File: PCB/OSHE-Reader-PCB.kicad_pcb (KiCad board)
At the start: 4 copper layers, 115 x 100 mm, 82 parts, among them J1 2171750001, J2 112L-TDA0, J3 Conn_01x24_MountingPin, J4 S2B-PH-K-SLFSN, Q1 PNP, Q2 Si1308EDL, SW1 SW_Push, SW2 SW_Push, SW3 SW_Push, SW4 SW_Push, SW5 SW_Push, U1 BQ2057CSNTR, U2 IRF7326D2TRPBF, U3 TPS5432DDA

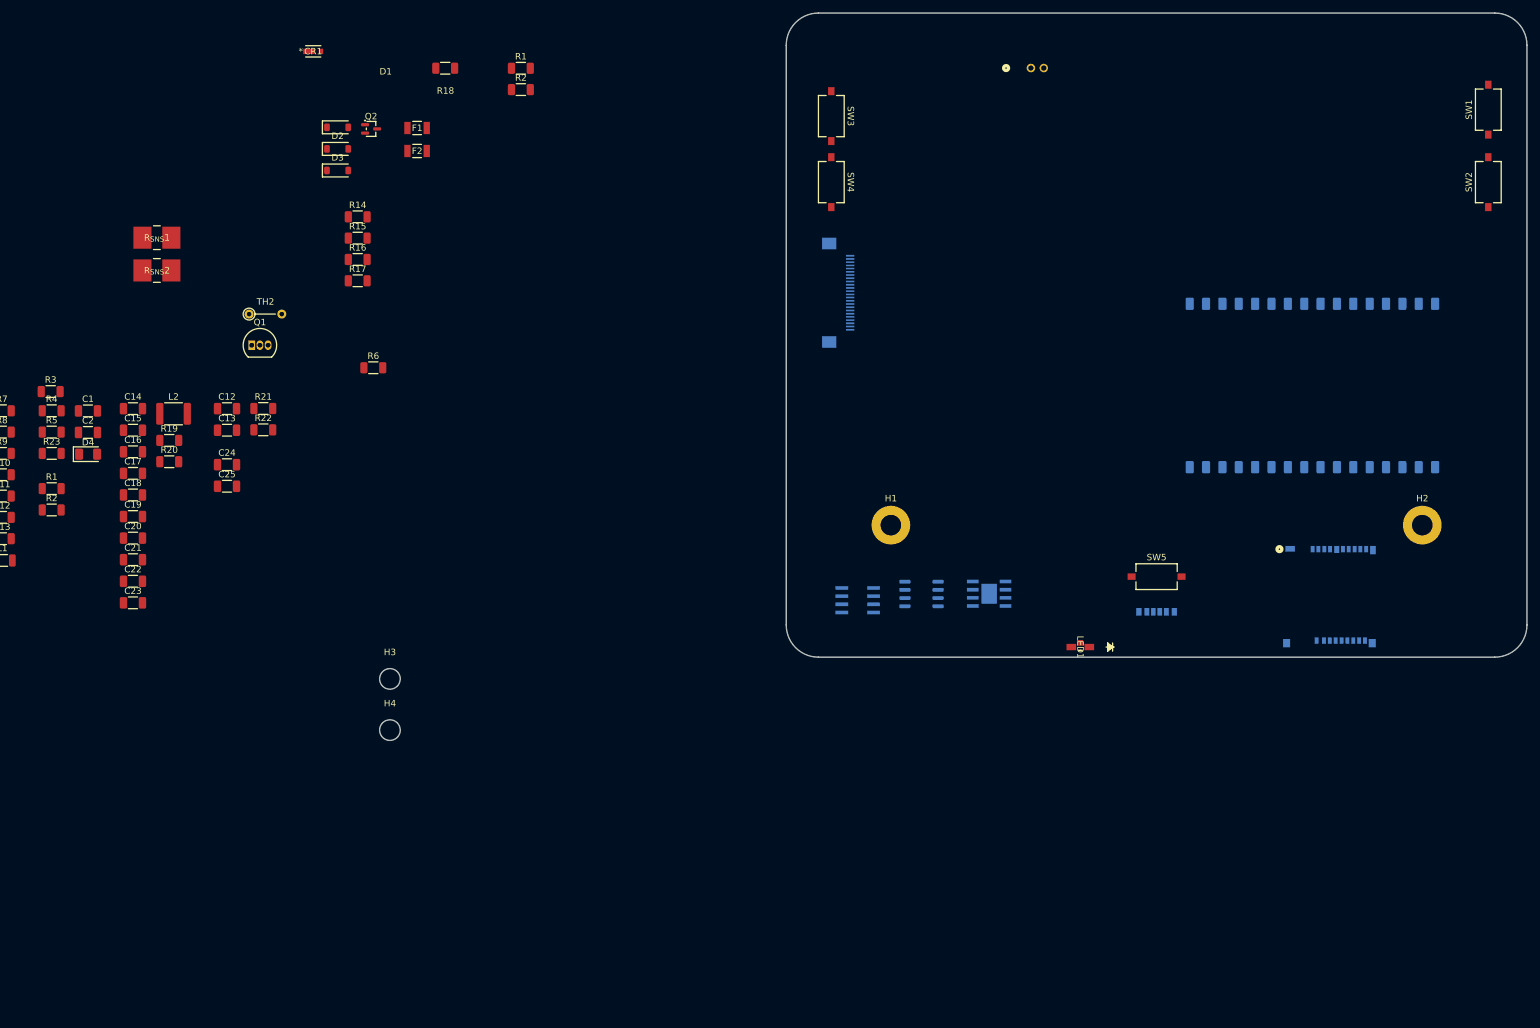
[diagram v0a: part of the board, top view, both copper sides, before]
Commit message: Started routing PCB & added case dxf for reference
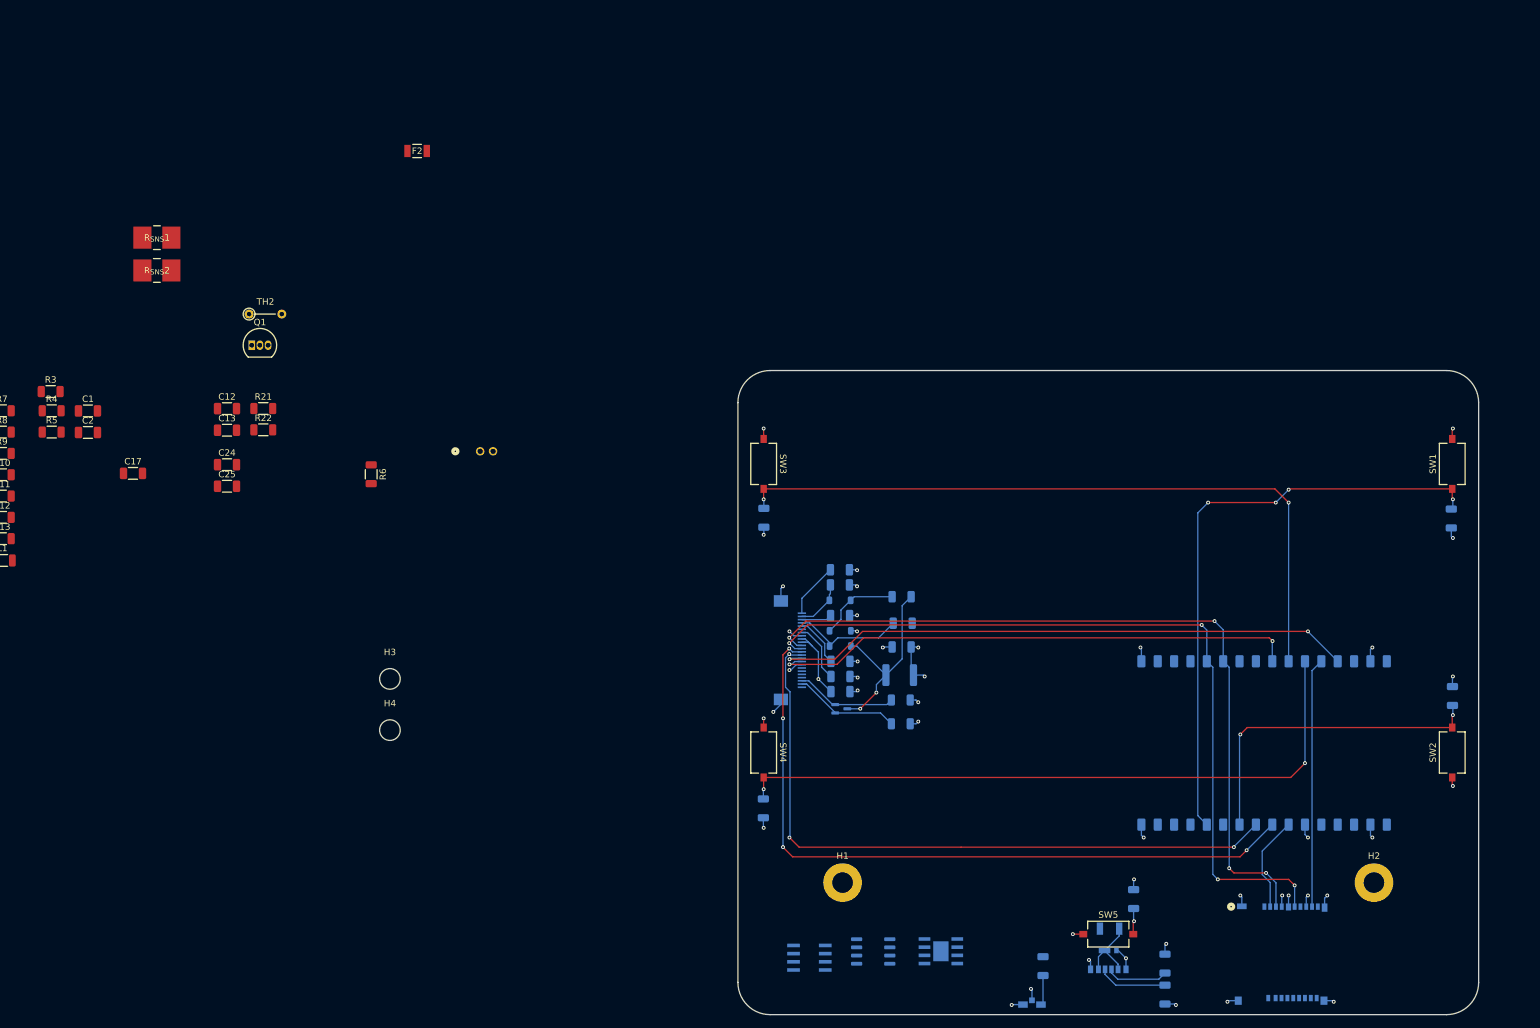
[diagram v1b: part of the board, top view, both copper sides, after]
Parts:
- removed D4: LED, LED_SMD:LED_1206_3216Metric
- removed the R1 at (-74.0, 98.8)
- removed the R2 at (-74.0, 102.1)
- C14, C15, C16, C18, C19, C20, C21, C22, C23, CR1, D1, D2, D3, F1, L2, LED1, Q2, R1, R14, R15, R16, R17, R18, R19, R2, R20, R23: moved to B.Cu
- moved CR1 186.4 mm to (90.1, 170.6)
- moved R17 181.8 mm to (143.4, 131.0), turned to 90 degrees
- moved R16 174.5 mm to (143.3, 103.5), turned to -90 degrees
- moved R23 173.3 mm to (79.9, 173.0), turned to -90 degrees
- moved R2 172.5 mm to (98.8, 177.4), turned to -90 degrees
- moved R1 171.2 mm to (98.8, 172.6), turned to -90 degrees
- moved R18 167.5 mm to (93.9, 162.6), turned to 90 degrees
- moved F1 164.3 mm to (90.2, 167.2), turned to 180 degrees
- moved C14 124.9 mm to (57.9, 123.4), turned to 180 degrees
- moved C15 123.2 mm to (58.1, 119.7)
- moved C16 121.4 mm to (57.9, 115.6)
- moved R20 120.6 mm to (57.8, 135.3)
- moved R19 120.5 mm to (57.8, 131.7)
- moved L2 119.8 mm to (57.6, 127.8), turned to 180 degrees
- moved Q2 115.9 mm to (48.5, 133.0)
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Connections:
- J3 pad 25: unconnected-(J3-Pad25) -> GND
- J3 pad 26: unconnected-(J3-Pad26) -> GND
- LED1 pad 2: unconnected-(LED1-Pad2) -> GND
- SW1 pad 1: +3V3 -> /Buttons/LeftButton
- SW1 pad 2: /Buttons/LeftButton -> +3V3
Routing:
- net /SCK: track 0.00 -> 123.7 mm, vias 0 -> 4
- net /COPI: track 0.00 -> 120.8 mm, vias 0 -> 4
- net /EP_CS: track 0.00 -> 112.1 mm, vias 0 -> 4
- net /Buttons/UpButton: track 0.00 -> 110.1 mm, vias 0 -> 2
- net /EP_D/C: track 0.00 -> 105.6 mm, vias 0 -> 3
- net /Buttons/DownButton: track 0.00 -> 104.1 mm, vias 0 -> 2
- net /Buttons/LeftButton: track 0.00 -> 93.3 mm, vias 0 -> 4
- net /EP_RESET: track 0.00 -> 91.0 mm, vias 0 -> 2
- net /EP_BUSY: track 0.00 -> 82.2 mm, vias 0 -> 2
- net GND: track 0.00 -> 61.5 mm, vias 0 -> 35
- net /Buttons/RightButton: track 0.00 -> 50.9 mm, vias 0 -> 2
- net /CIPO: track 0.00 -> 38.7 mm
- net +3V3: track 0.00 -> 31.3 mm, vias 0 -> 10
- net Net-(D2-A): track 0.00 -> 30.0 mm, vias 0 -> 2
- net /Display Connector/PREVGH: track 0.00 -> 17.4 mm
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
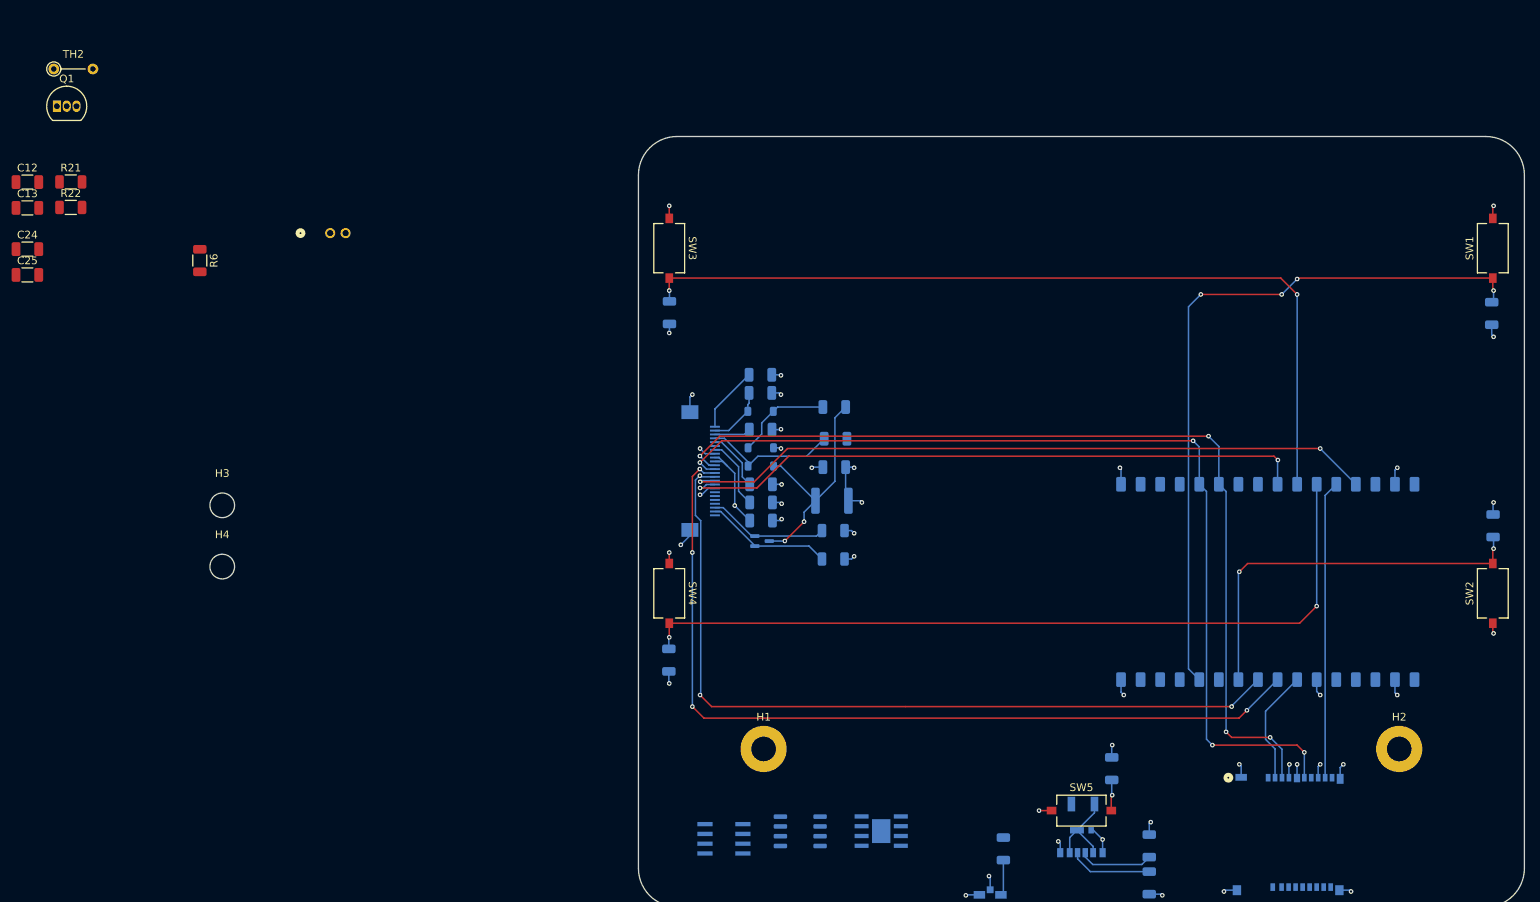
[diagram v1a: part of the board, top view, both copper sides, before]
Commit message: More work done on PCB. TODO: Battery Charging and Buck Converter
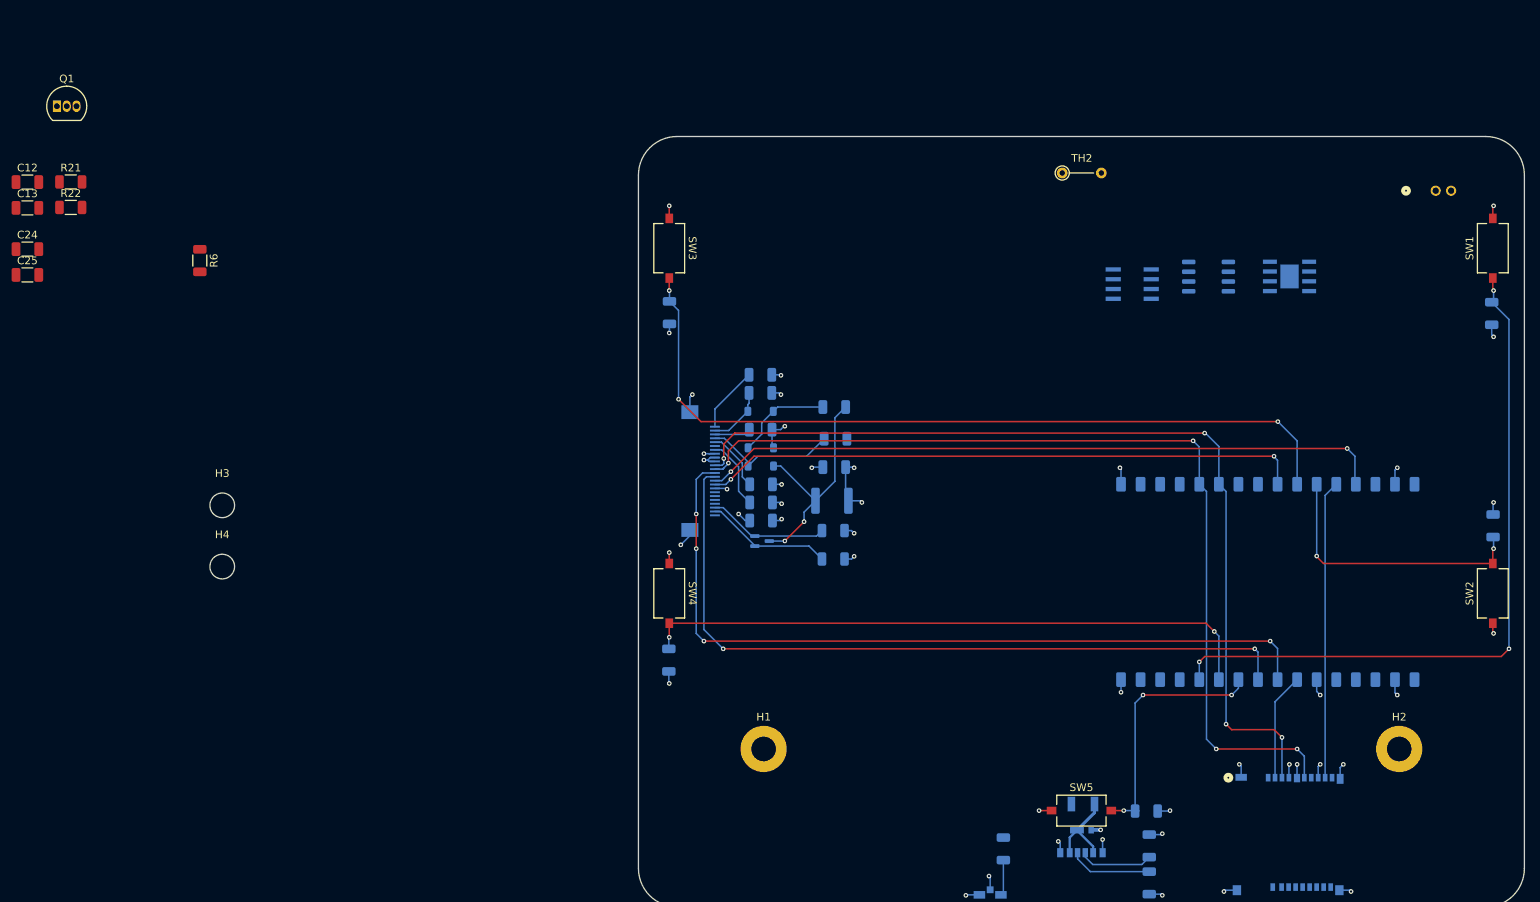
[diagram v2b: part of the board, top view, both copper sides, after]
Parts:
- moved J4 143.6 mm to (136.0, 87.5)
- moved TH2 131.6 mm to (87.5, 85.2)
- moved U1 89.4 mm to (96.6, 99.7)
- moved U2 89.4 mm to (106.5, 98.7)
- moved U3 89.4 mm to (117.0, 98.7)
- moved R18 7.11 mm to (98.4, 168.1), turned to 0 degrees
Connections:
- U4 pad 11: /Buttons/DownButton -> /Buttons/RightButton
- U4 pad 22: /Buttons/HomeButton -> /Buttons/DownButton
- U4 pad 23: /Buttons/RightButton -> /Buttons/HomeButton
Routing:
- net /Buttons/HomeButton: track 4.06 -> 33.0 mm, vias 1 -> 3
- net /Buttons/DownButton: track 104.1 -> 81.0 mm
- net /Buttons/RightButton: track 50.9 -> 36.1 mm
- net /EP_CS: track 112.1 -> 103.1 mm
- net /EP_D/C: track 105.6 -> 97.8 mm, vias 3 -> 2
- net +3V3: track 31.3 -> 24.0 mm, vias 10 -> 11
- net /Buttons/UpButton: track 110.1 -> 104.4 mm, vias 2 -> 3
- net /EP_BUSY: track 82.2 -> 77.9 mm
- net /SCK: track 123.7 -> 120.6 mm
- net /EP_RESET: track 91.0 -> 88.9 mm
- net /COPI: track 120.8 -> 119.0 mm
- net /SD_CS: track 14.9 -> 13.9 mm
- net /Buttons/LeftButton: track 93.3 -> 92.4 mm, vias 4 -> 3
- net GND: track 61.5 -> 61.0 mm

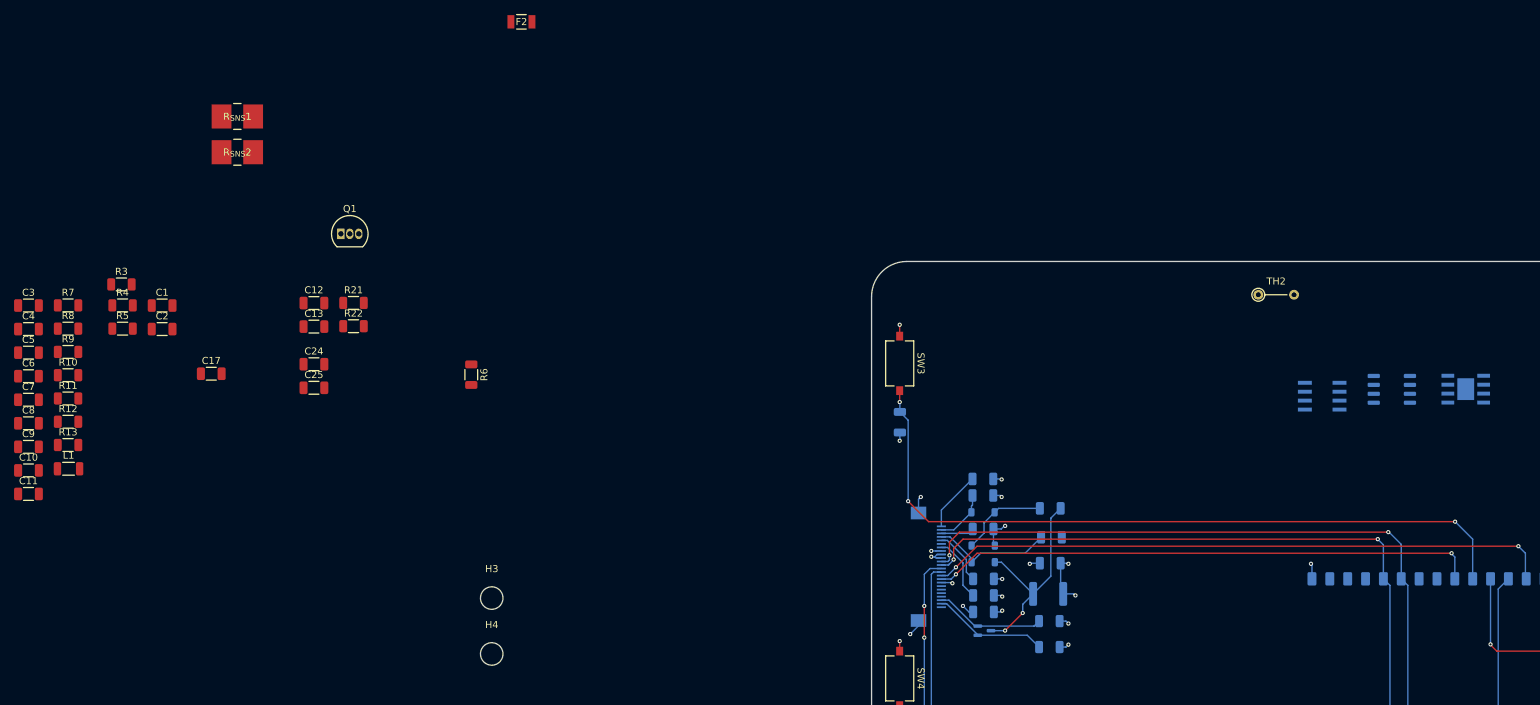
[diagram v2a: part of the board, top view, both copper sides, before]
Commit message: Updated PCB
Did some work on the PCB, placing footprints
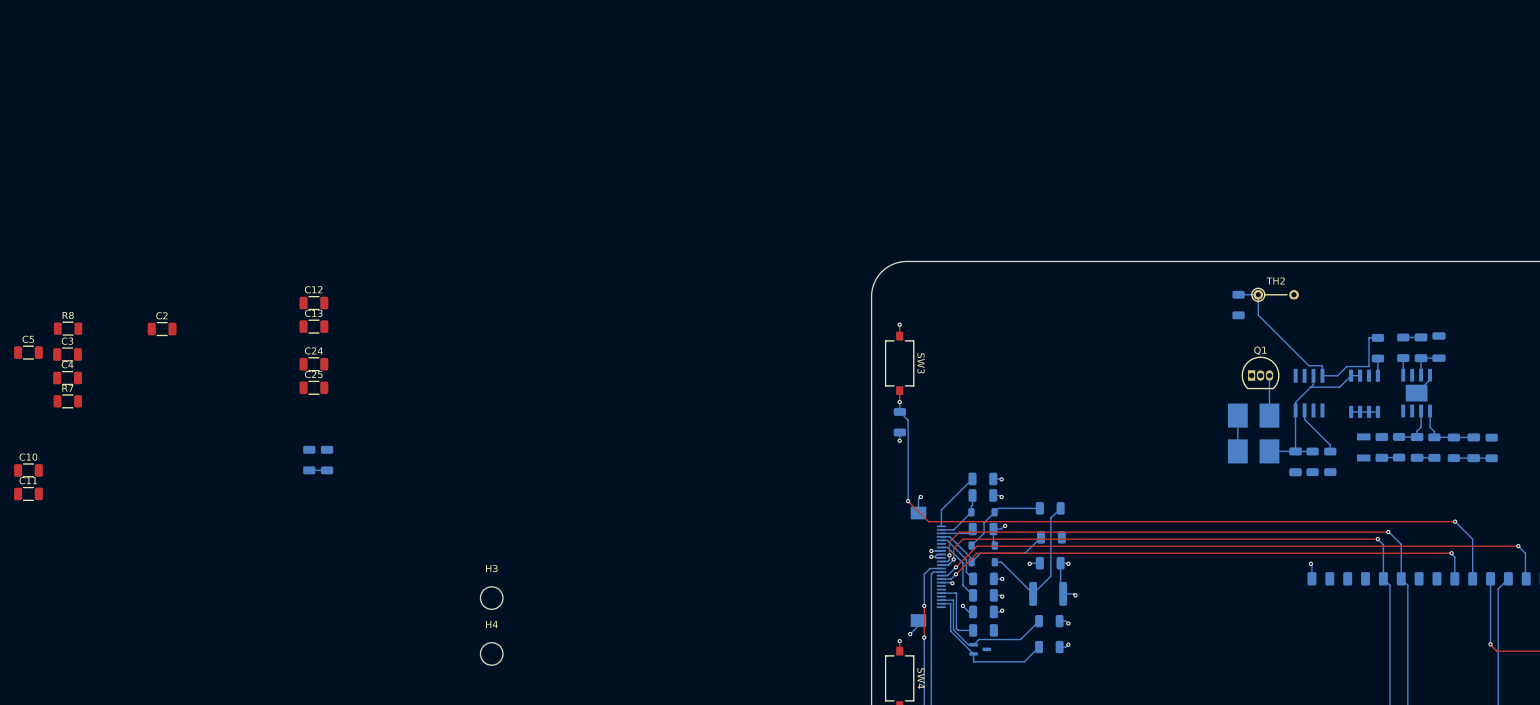
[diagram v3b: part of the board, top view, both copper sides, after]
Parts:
- C1, C17, C6, C7, C8, C9, F2, L1, R10, R11, R12, R13, R21, R22, R3, R4, R5, R6, R9, R_{SNS}1, R_{SNS}2: moved to B.Cu
- moved C9 205.6 mm to (118.2, 107.0), turned to -90 degrees
- moved R11 202.6 mm to (120.7, 107.0), turned to -90 degrees
- moved C8 198.4 mm to (110.7, 92.8), turned to 90 degrees
- moved C7 197.6 mm to (110.1, 107.0), turned to -90 degrees
- moved R12 197.1 mm to (115.3, 107.0), turned to 90 degrees
- moved L1 195.7 mm to (113.2, 92.7), turned to 90 degrees
- moved R13 194.3 mm to (112.5, 107.0), turned to -90 degrees
- moved C6 192.8 mm to (105.1, 107.0), turned to 90 degrees
- moved R10 190.0 mm to (108.1, 92.8), turned to -90 degrees
- moved R9 189.8 mm to (107.5, 106.9), turned to -90 degrees
- moved R3 179.0 mm to (104.5, 92.8), turned to 90 degrees
- moved R5 172.8 mm to (97.8, 109.0), turned to 90 degrees
- moved C1 162.7 mm to (92.8, 109.0), turned to -90 degrees
- moved R4 158.7 mm to (84.7, 86.7), turned to -90 degrees
- moved R_{SNS}1 152.2 mm to (86.8, 107.5), turned to 180 degrees
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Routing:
- net /Battery Charging/TS: track 0.00 -> 31.8 mm
- net /Battery Charging/VBUS: track 0.00 -> 28.1 mm
- net Net-(J3-VSHR): track 0.00 -> 9.70 mm
- net /Buck Converter/5: track 0.00 -> 9.61 mm
- net Net-(D2-A): track 30.0 -> 21.1 mm, vias 2 -> 0
- net Net-(U1-CC): track 0.00 -> 7.36 mm
- net /Buck Converter/6: track 0.00 -> 6.51 mm
- net GND: track 61.0 -> 66.8 mm
- net Net-(Q1-E): track 0.00 -> 5.70 mm
- net Net-(C9-Pad2): track 0.00 -> 5.39 mm
- net Net-(R_{SNS}1-Pad2): track 0.00 -> 5.09 mm
- net /Buck Converter/3: track 0.00 -> 4.98 mm
- net /Display Connector/GDR: track 16.5 -> 21.1 mm
- net /Display Connector/RESE: track 15.7 -> 20.4 mm
- net /Battery Charging/VOUT: track 0.00 -> 3.81 mm
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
